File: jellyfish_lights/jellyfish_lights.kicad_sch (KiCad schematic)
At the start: 24 parts, among them Q1 AO3400A, SW1 tilt switch, U1 SN74LVC1G14DBV

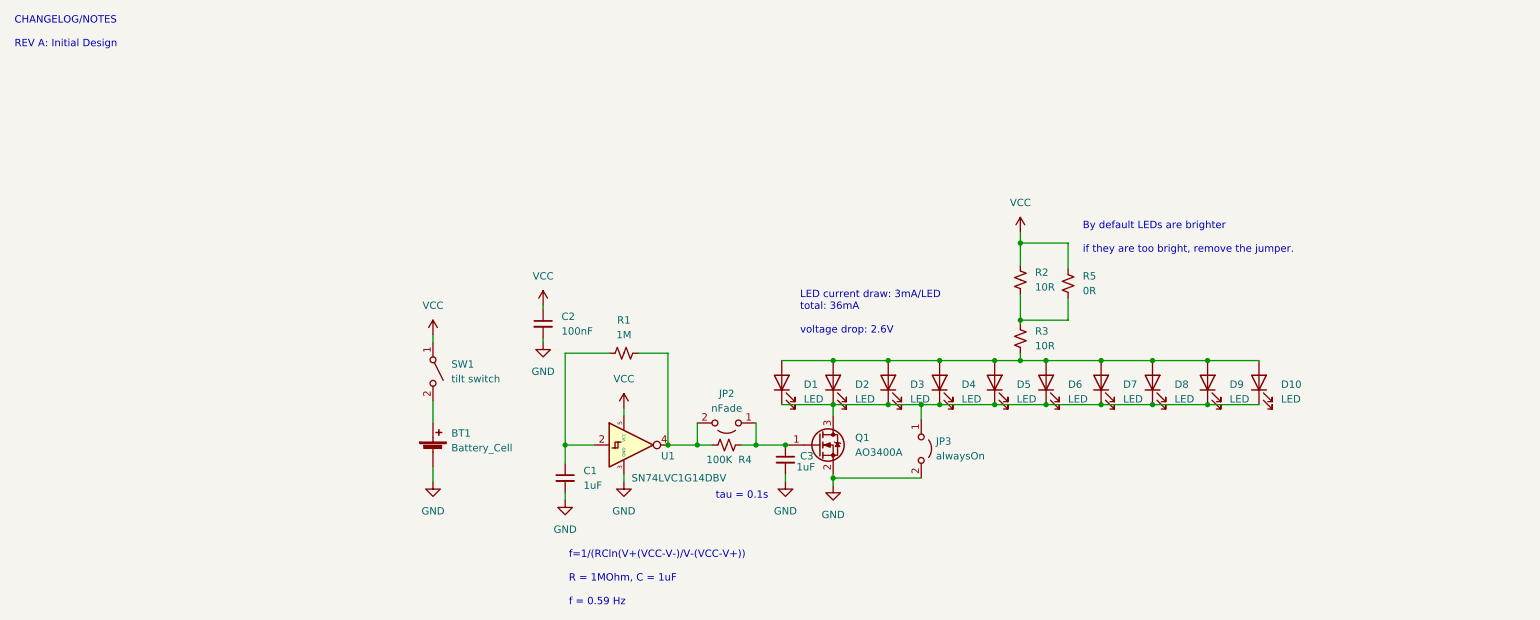
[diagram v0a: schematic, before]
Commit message: created B01
B01 has a new circuit to do blinking. The op-amp allows for fading of the lights
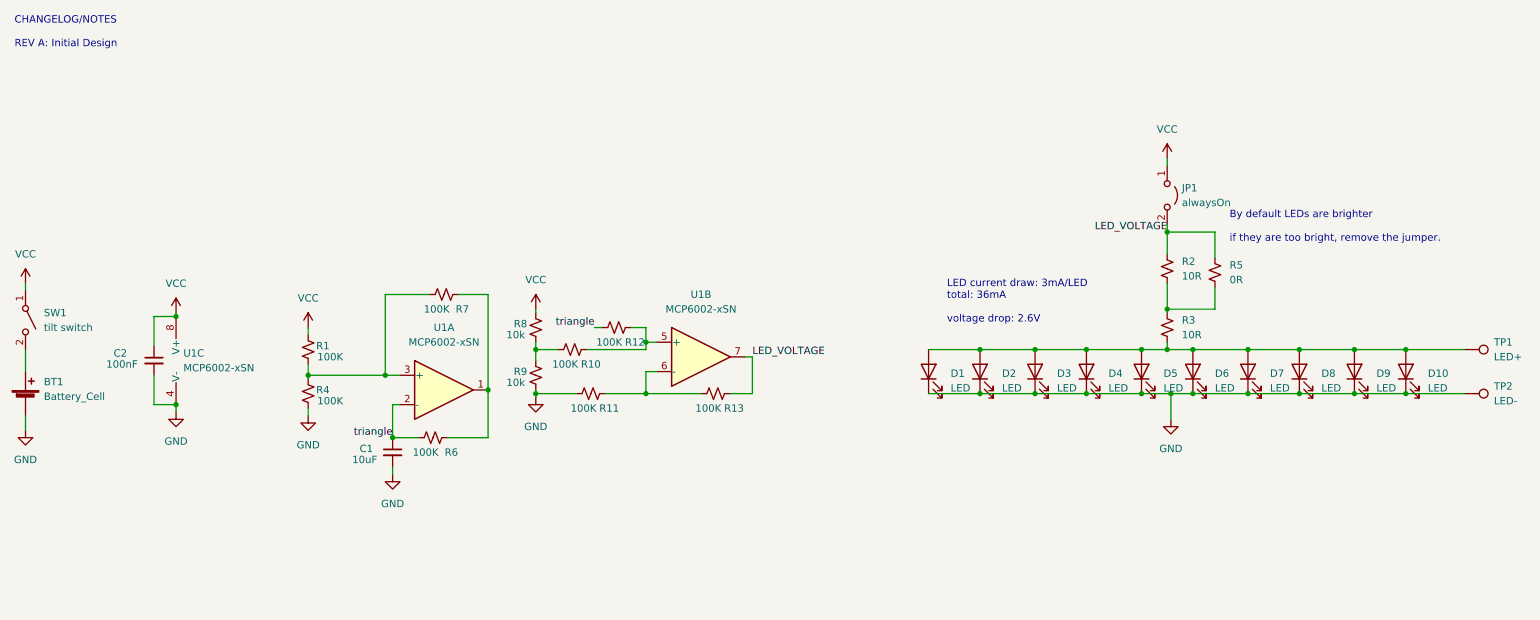
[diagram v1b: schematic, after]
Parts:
- removed C3: 1uF, Capacitor_SMD:C_0402_1005Metric, symbol Device:C_Small
- removed JP2: nFade, Jumper:SolderJumper-2_P1.3mm_Open_TrianglePad1.0x1.5mm, symbol Jumper:Jumper_2_Open
- removed JP3: alwaysOn, Jumper:SolderJumper-2_P1.3mm_Open_TrianglePad1.0x1.5mm, symbol Jumper:Jumper_2_Open
- removed Q1: AO3400A, Package_TO_SOT_SMD:SOT-23, symbol Transistor_FET:AO3400A
- removed U1: SN74LVC1G14DBV, Package_TO_SOT_SMD:SOT-23-5, symbol 74xGxx:SN74LVC1G14DBV
- added JP1: alwaysOn, Jumper:SolderJumper-2_P1.3mm_Open_TrianglePad1.0x1.5mm, symbol Jumper:Jumper_2_Open
- added R10, R11, R12, R13, R6, R7: 100K, Resistor_SMD:R_0402_1005Metric, symbol Device:R_Small_US
- added R8, R9: 10k, Resistor_SMD:R_0402_1005Metric, symbol Device:R_Small_US
- added TP1: LED+, TestPoint:TestPoint_THTPad_D2.0mm_Drill1.0mm, symbol Connector:TestPoint
- added TP2: LED-, TestPoint:TestPoint_THTPad_D2.0mm_Drill1.0mm, symbol Connector:TestPoint
- added U1: MCP6002-xSN, Package_SO:SOIC-8_3.9x4.9mm_P1.27mm, symbol Amplifier_Operational:MCP6002-xSN
- BT1: footprint Battery:BatteryHolder_Keystone_3002_1x2032 -> Battery:BatteryHolder_MPD_BC2003_1x2032
- C1: value 1uF -> 10uF; LCSC C52923 -> C15525
- R1: value 1M -> 100K; LCSC C26083 -> C25741
- R2, R3: footprint Resistor_SMD:R_0603_1608Metric -> Resistor_SMD:R_0402_1005Metric
- R5: footprint Resistor_SMD:R_0603_1608Metric -> Jumper:SolderJumper-2_P1.3mm_Open_TrianglePad1.0x1.5mm; LCSC C17168 -> (none)
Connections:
- net GND: now also D1.1 (K), D10.1 (K), D2.1 (K), D3.1 (K), D4.1 (K), D5.1 (K), D6.1 (K), D7.1 (K), D8.1 (K), D9.1 (K), R4.1, R11.1, R9.2, TP2.1, U1.4 (V-)
- net VCC: now also R1.2, JP1.1 (A), R8.1, U1.8 (V+); no longer R2.1, R5.1
- net at D1.2 (A), D10.2 (A), D2.2 (A)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: now also TP1.1
- net at R4.2: now also R1.1, R7.1, U1.3 (+)
- net triangle: now reaches C1.1
- net triangle: now also R12.1, R6.1, U1.2 (-); no longer R1.1
- new net: R10.1, R8.2, R9.1
- new net: R10.2, R12.2, U1.5 (+)
- new net: R11.2, R13.1, U1.6 (-)
- new net: R6.2, R7.2, U1.1
- new net LED_VOLTAGE: JP1.2 (B), R13.2, R2.1, R5.1, U1.7
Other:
- note removed: "f=1/(RCln(V+(VCC-V-)/V-(VCC-V+)) R = 1MOhm, C = 1uF f = 0.59 Hz"
- note removed: "tau = 0.1s"
- title: Main -> Jellyfish Lights
- moved on the sheet: BT1, C2, D1, D10, D2, D3, D4, D5, D6, D7, D8, D9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
